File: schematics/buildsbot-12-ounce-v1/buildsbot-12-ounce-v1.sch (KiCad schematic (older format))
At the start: 15 parts

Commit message: Continued working on schematic
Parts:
- added C?: 1 uF, symbol C
- added C? (x4): .1uF, symbol C
- added P?: CONN_10, symbol CONN_10
- added R?: 10K, symbol R
- added R?: 1K, symbol R
- added S?: MOM-PUSHBUTTON, symbol MOM-PUSHBUTTON
- C?: value .33 uF -> .33uF
- C?: value .1 uF -> .1uF
- C?: value .1 uF -> 10pF
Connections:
- net +5V: now also J?.2, C?.1, P?.1 (P1), R?.2; no longer U?.7 (VBUS)
- net GND: now also C?.2, J?.6, C?.2, C?.2, C?.2, C?.2, C?.2, P?.2 (P2), R?.1, S?.3, S?.4; no longer C?.1
- net MISO: now reaches J?.1
- net MISO: now also U?.11 (PB3(PDO/MISO))
- net SCK: now reaches J?.3
- net SCK: now also U?.9 (PB1(SCK))
- net MOSI: now reaches J?.4
- net MOSI: now also U?.10 (PB2(PDI/MOSI))
- net RESET: now reaches J?.5
- net RESET: now also U?.13 (/RESET), R?.1, S?.1, S?.2
- net at J?.1 (P1), J?.VBUS: now also C?.1, U?.7 (VBUS); no longer C?.2
- net at U?.1 (PE6): now also P?.9 (P9)
- net at U?.33 (PE2(HWB)): now also R?.2
- net at U?.36 (PF7(ADC7(TDI)): now also P?.8 (P8)
- net at U?.37 (PF6(ADC6/TDO)): now also P?.7 (P7)
- net at U?.38 (PF5(ADC5/TMS)): now also P?.6 (P6)
- net at U?.39 (PF4(ADC4/TCK)): now also P?.5 (P5)
- net at U?.40 (PF1(ADC1)): now also P?.4 (P4)
- net at U?.41 (PF0(ADC0)): now also P?.3 (P3)
- net AREF: now reaches U?.42 (AREF)
- net AREF: now also P?.10 (P10)
- net at U?.6 (UCAP): now also C?.1
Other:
- note removed: "(NOTE: use jumper to select if using \nUSB power or Battery/External power)\n"
- moved on the sheet: C?, J?, P?, R?, U?, X?

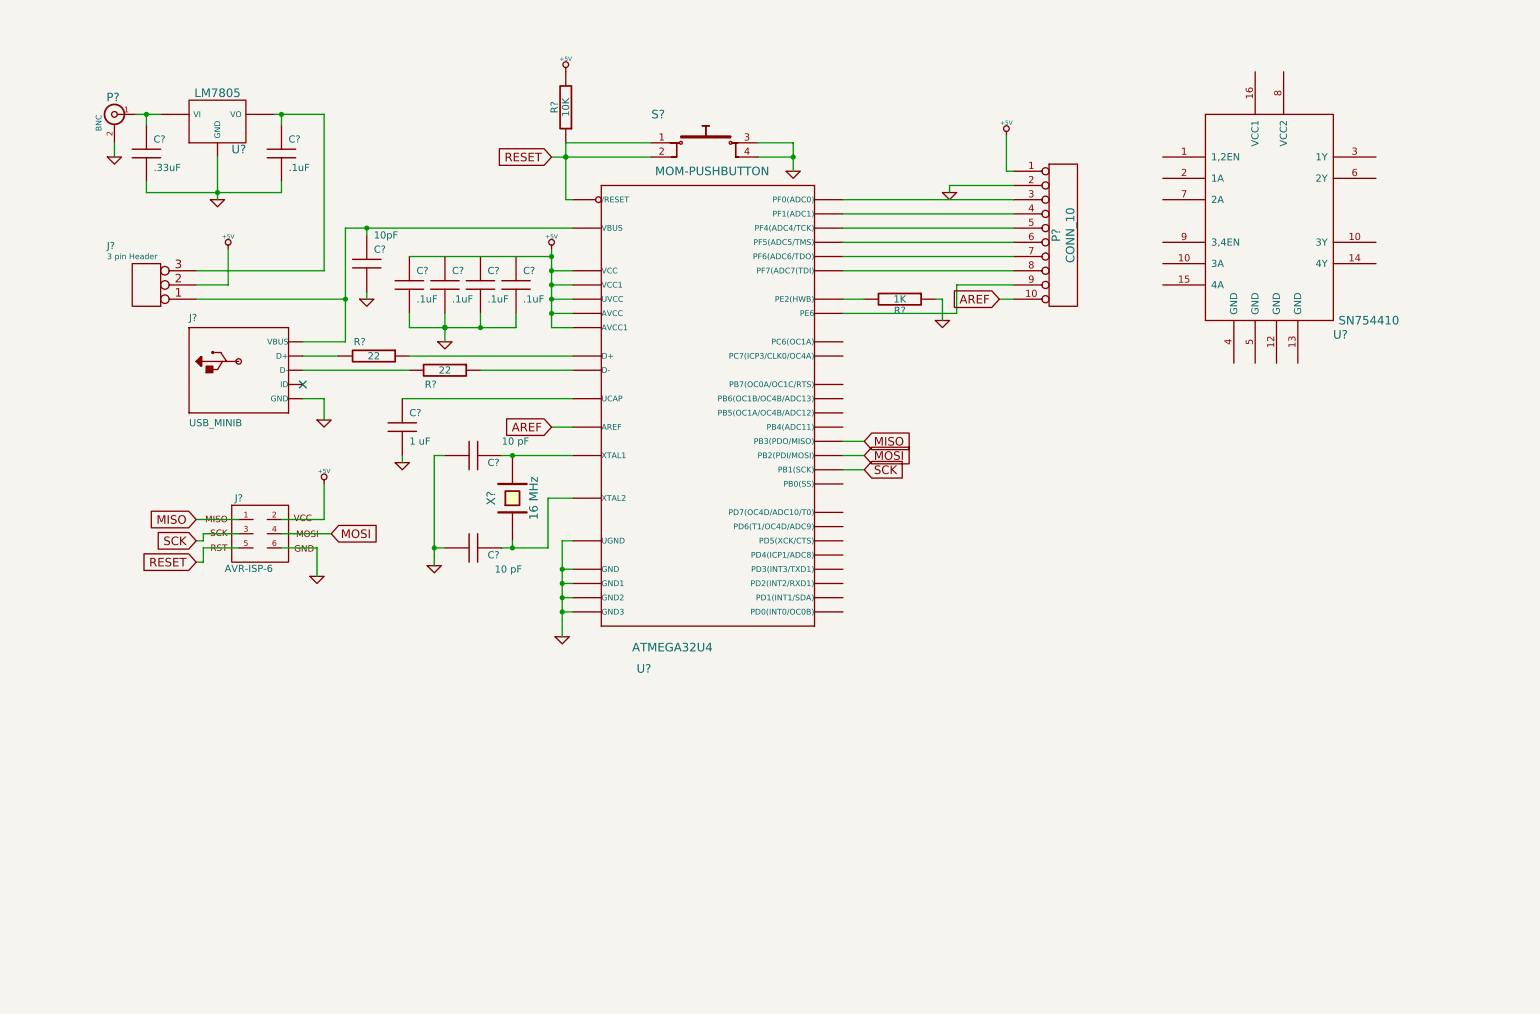
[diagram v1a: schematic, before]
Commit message: Decided to use 74HC14 Hex Schmitt Trigger Inverters to use only one pin for each motor direction control (2 pins for each motor now: enable and direction). Also, Terminal blocks. Trying to decide on pinout. Then send schematic out for review by Dan, John, Eric, etc... Then do PCB layout, find a production house we like (possibly SeeedStudio, who does real cheap PCB production... Or 4pcb.com or one of those other ones. Look for a quick turn & low quantity so that errors can be spoted and fixed.
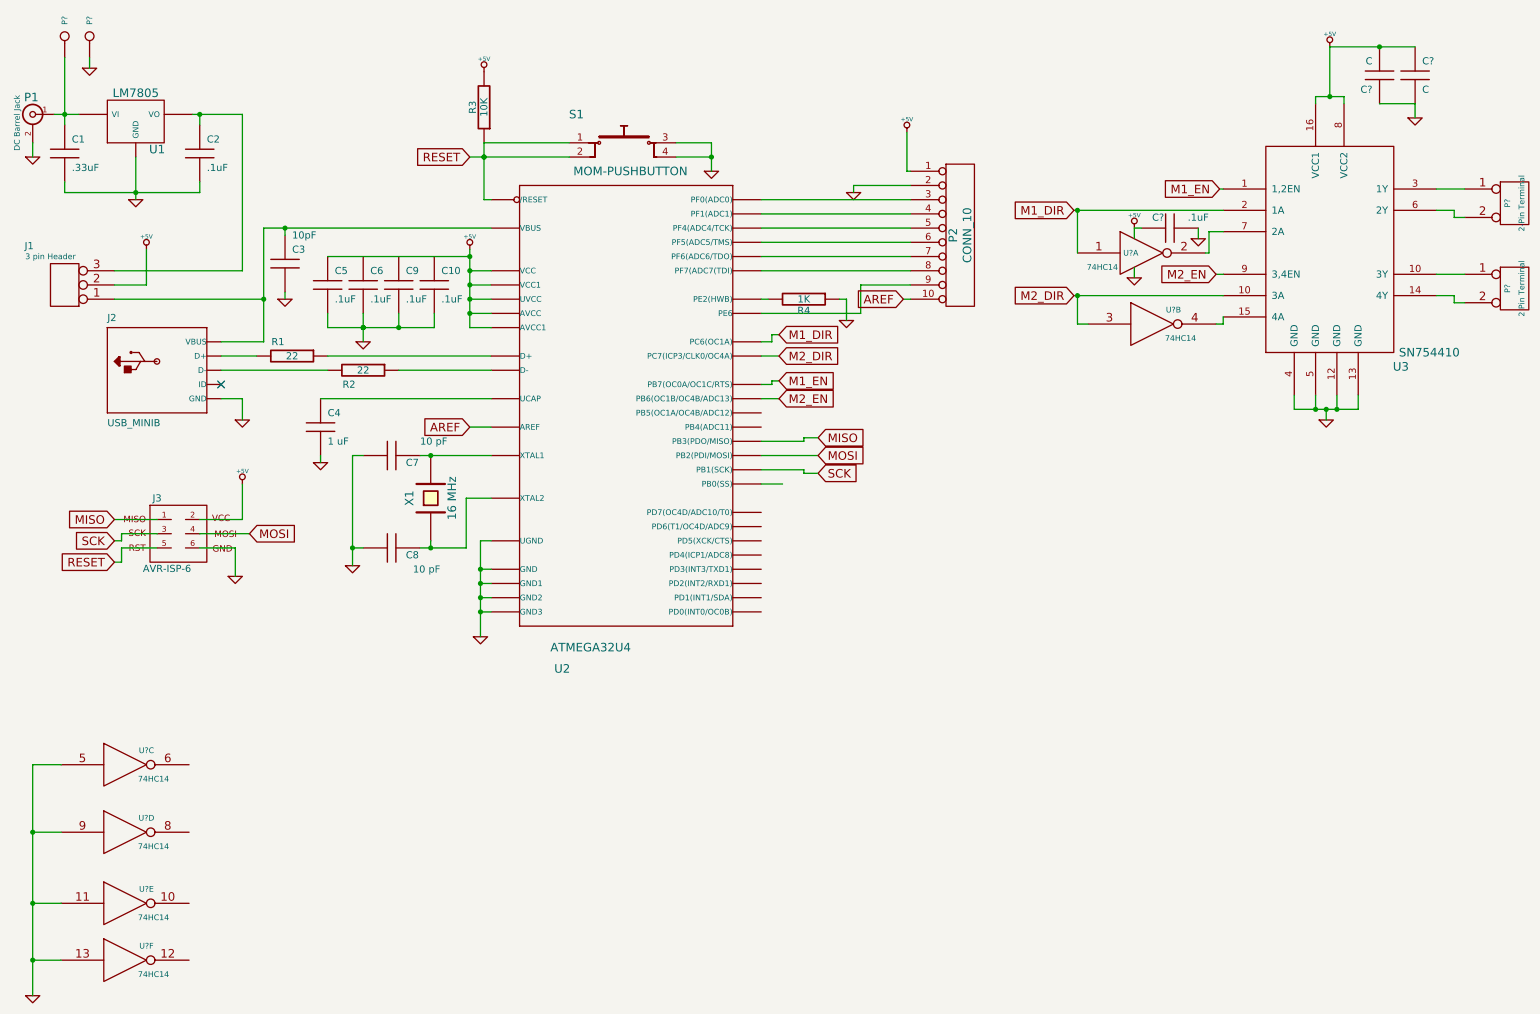
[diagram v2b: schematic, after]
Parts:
- added C?: .1uF, symbol C
- added C? (x2): C, symbol C
- added P?: 2-Pin Terminal, symbol CONN_2
- added P?: 2 Pin Terminal, symbol CONN_2
- added P? (x2): CONN_1, symbol CONN_1
- added U? (x6): 74HC14, symbol 74HC14
- P1: renamed from P?; value BNC -> DC Barrel Jack
- gave numbers to parts that had none: 23
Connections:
- net +5V: now also U3.16 (VCC1), U3.8 (VCC2), C?.1, C?.2, C?.2, U?.14 (VCC), U?.14 (VCC), U?.14 (VCC), U?.14 (VCC), U?.14 (VCC), U?.14 (VCC)
- net GND: now also U3.12 (GND), U3.13 (GND), U3.4 (GND), U3.5 (GND), C?.1, C?.1, C?.2, P?.1, U?.11, U?.13, U?.5, U?.7 (GND), U?.7 (GND), U?.7 (GND), U?.7 (GND), U?.7 (GND), U?.7 (GND), U?.9
- net M1_EN: now reaches U3.1 (1,2EN)
- net M1_EN: now also U2.12 (PB7(OC0A/OC1C/RTS))
- net M2_DIR: now reaches U3.10 (3Y)
- net M2_DIR: now also U2.32 (PC7(ICP3/CLK0/OC4A)), U?.3
- net at U3.14 (4Y): now also P?.2 (PM)
- net at U3.15 (4A): now also U?.4
- net M1_DIR: now reaches U3.2 (1A)
- net M1_DIR: now also U2.31 (PC6(OC1A)), U?.1
- net at U3.3 (1Y): now also P?.1 (P1)
- net at U3.6 (2Y): now also P?.2 (PM)
- net at U3.7 (2A): now also U?.2
- net M2_EN: now reaches U3.9 (3,4EN)
- net M2_EN: now also U2.30 (PB6(OC1B/OC4B/ADC13))
- net at C1.1, P1.1 (In), U1.VI: now also P?.1
- new net: P?.1 (P1), U3.10 (3Y)
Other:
- moved on the sheet: C1, C10, C2, C3, C4, C5, C6, C7, C8, C9, J1, J2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

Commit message: Added connector for Sparkfun FTDI UART. Also made global smaller (to .05 instead of .06... Makes everything cleaner) Need to add 2 Servo motor connectors or PWM pins, I2C bus output
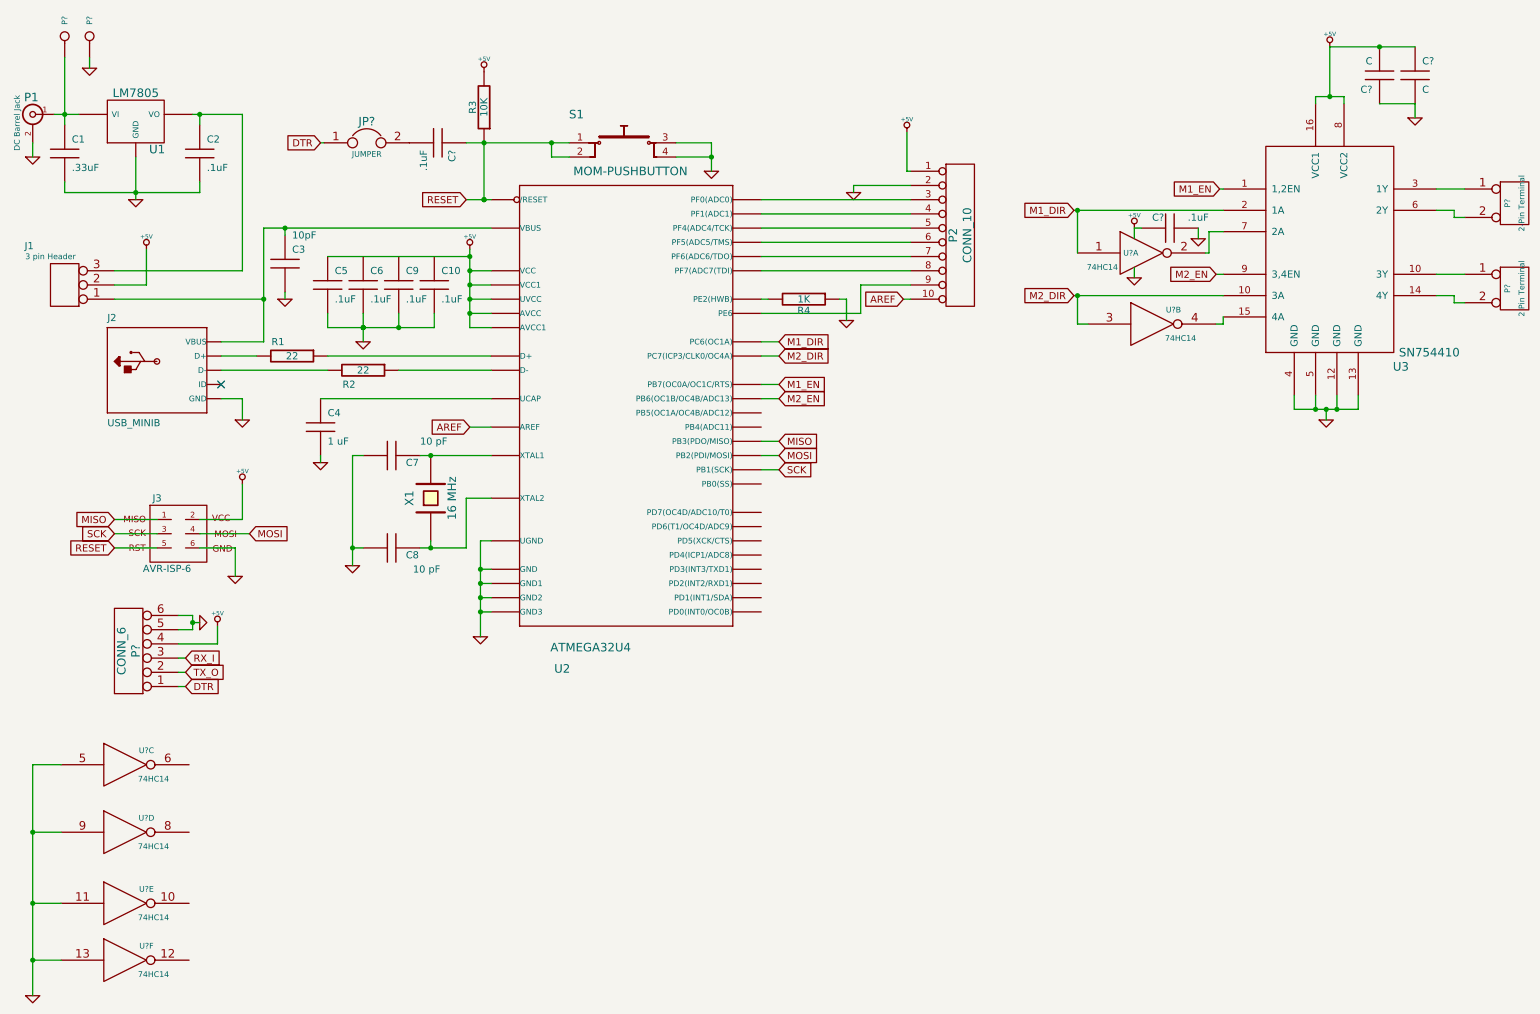
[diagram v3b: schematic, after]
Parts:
- added C?: .1uF, symbol C
- added JP?: JUMPER, symbol JUMPER
- added P?: CONN_6, symbol CONN_6
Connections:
- net +5V: now also P?.4
- net GND: now also P?.5, P?.6
- net RESET: now also C?.1
- new net: C?.2, JP?.2
- new net DTR: JP?.1, P?.1
- new net RX_I: P?.3
- new net TX_O: P?.2

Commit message: Made new 3 pin jumper schematic symbol. Added 2 servo outputs. Made phototransistor symbol
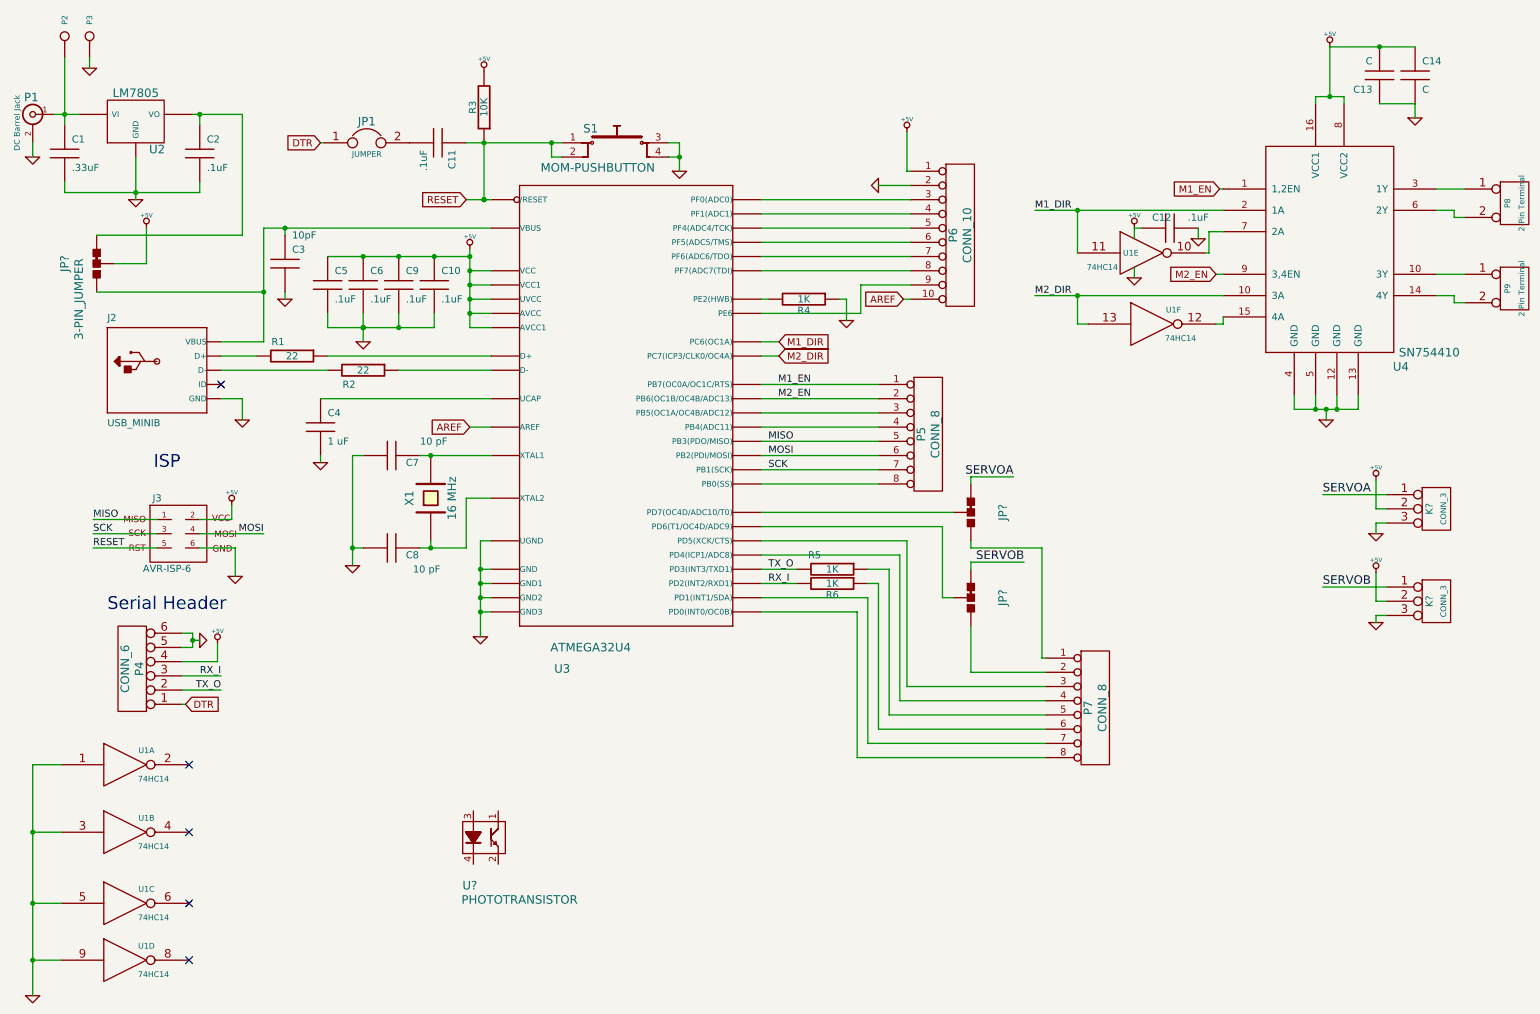
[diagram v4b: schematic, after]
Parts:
- removed J1: 3 pin Header, symbol CONN_3
- added JP? (x3): 3-PIN_JUMPER, symbol 3-PIN_JUMPER
- added K? (x2): CONN_3, symbol CONN_3
- added P5, P7: CONN_8, symbol CONN_8
- added R5, R6: 1K, symbol R
- added U?: PHOTOTRANSISTOR, symbol PHOTOTRANSISTOR
- gave numbers to parts that had none: 11
- renumbered P2 to P6, U1 to U2, U2 to U3, U3 to U4
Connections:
- net +5V: now also C10.1, C6.1, C9.1, JP?.2, K?.2 (PM), K?.2 (PM)
- net GND: now also U1.1, U1.3, U1.5, U1.9, K?.3 (P3), K?.3 (P3); no longer U1.11, U1.13, U1.5, U1.9
- net M1_DIR: now also U1.11; no longer U1.1
- net M1_EN: now also P5.1 (P1)
- net M2_DIR: now also U1.13; no longer U1.3
- net M2_EN: now also P5.2 (P2)
- net MISO: now also P5.5 (P5)
- net MOSI: now also P5.6 (P6)
- net RX_I: now also U3.20 (PD2(INT2/RXD1)), R6.2
- net SCK: now also P5.7 (P7)
- net TX_O: now also U3.21 (PD3(INT3/TXD1)), R5.2
- net at U4.15 (4A): now also U1.12; no longer U1.4
- net at U4.7 (2A): now also U1.10; no longer U1.2
- net at C3.1, J2.VBUS, U3.7 (VBUS): now also JP?.2
- net at U3.18 (PD0(INT0/OC0B)): now also P7.8 (P8)
- net at U3.19 (PD1(INT1/SDA)): now also P7.7 (P7)
- net at U3.22 (PD5(XCK/CTS)): now also P7.3 (P3)
- net at U3.25 (PD4(ICP1/ADC8)): now also P7.4 (P4)
- net at U3.26 (PD6(T1/OC4D/ADC9)): now also JP?.2
- net at U3.27 (PD7(OC4D/ADC10/T0)): now also JP?.2
- net at U3.28 (PB4(ADC11)): now also P5.4 (P4)
- net at U3.29 (PB5(OC1A/OC4B/ADC12)): now also P5.3 (P3)
- net at U3.8 (PB0(SS)): now also P5.8 (P8)
- net at C2.1, U2.VO: now also JP?.1
- new net: P7.5 (P5), R5.1
- new net: P7.6 (P6), R6.1
- new net: JP?.2, P7.1 (P1)
- new net: JP?.2, P7.2 (P2)
- new net SERVOA: JP?.1, K?.1 (P1)
- new net SERVOB: JP?.1, K?.1 (P1)
- no-connect marks 1 -> 5
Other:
- note added: "ISP"
- note added: "Serial Header"
- moved on the sheet: P4, S1
